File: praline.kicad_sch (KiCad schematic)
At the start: 0 parts

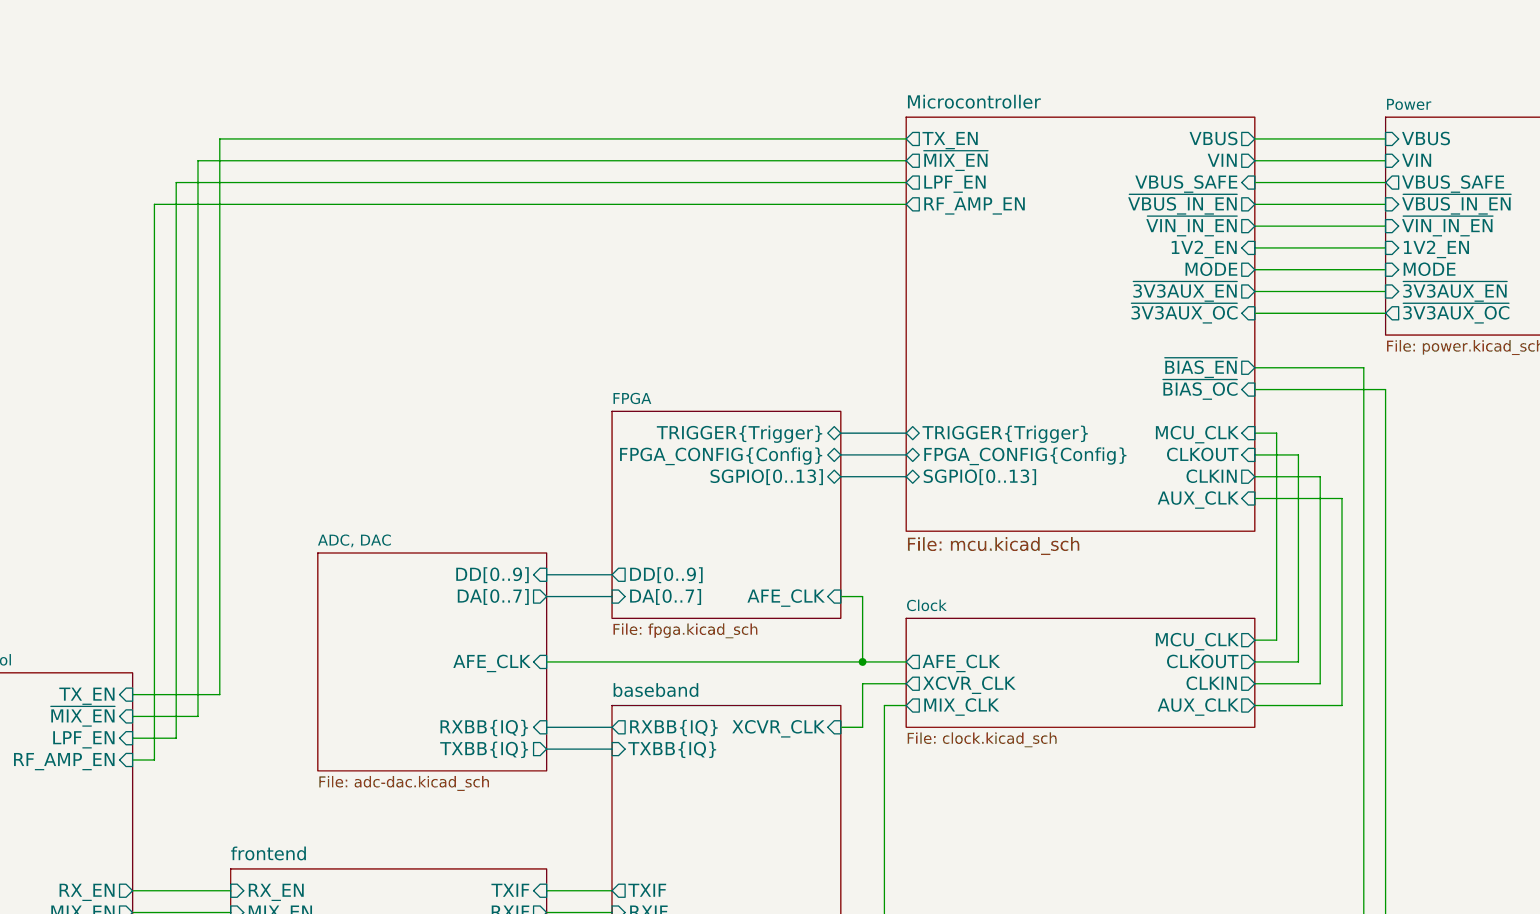
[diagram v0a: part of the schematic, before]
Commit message: Add Type-C controller
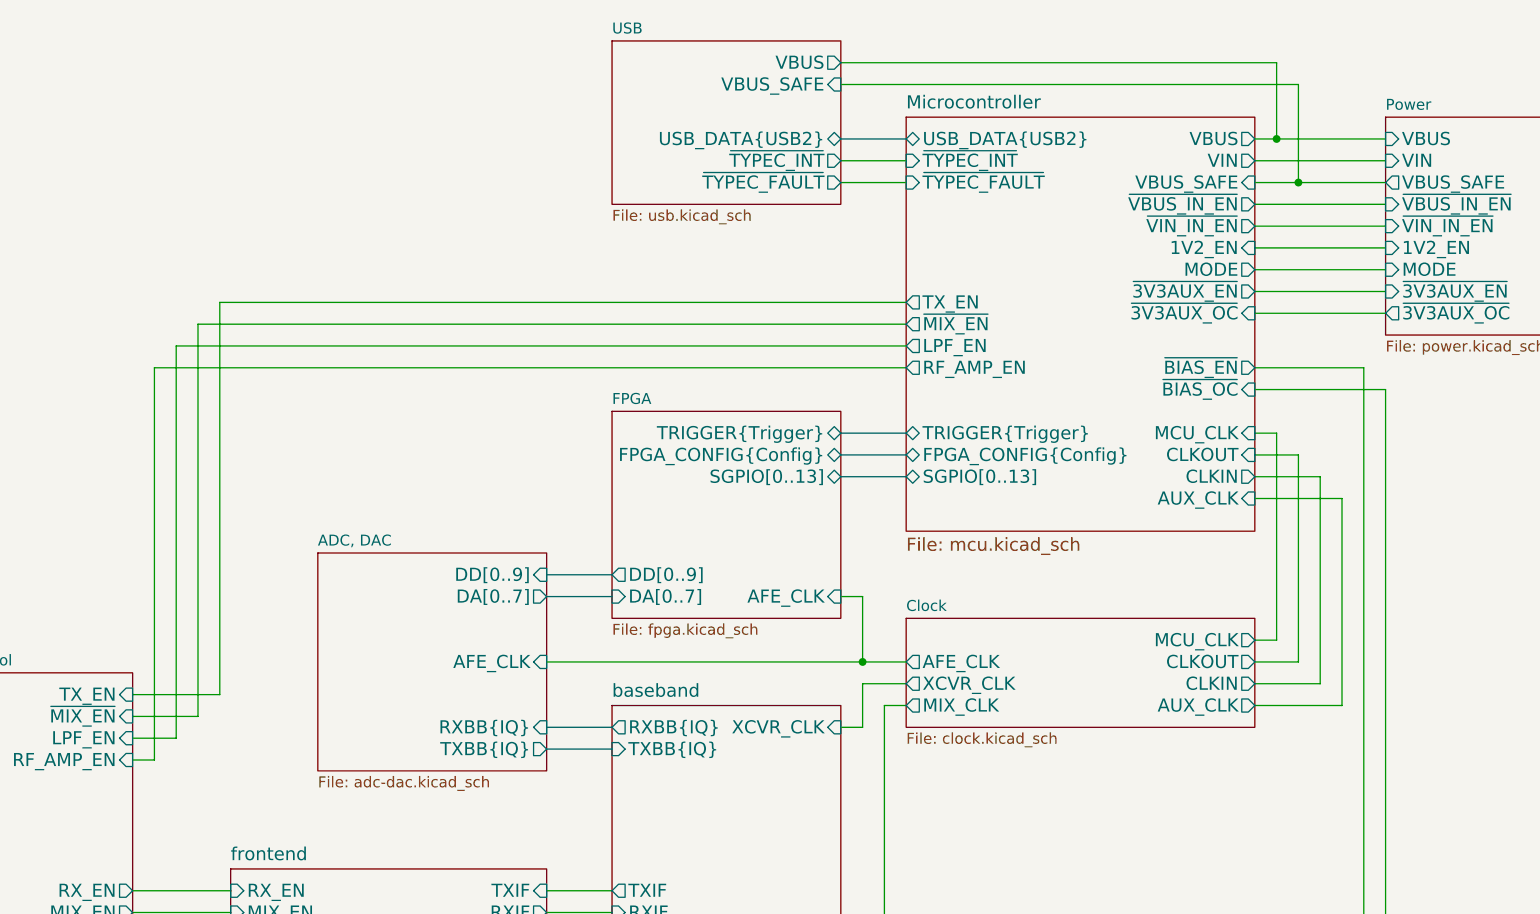
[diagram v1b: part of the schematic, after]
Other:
- added sheet USB (usb.kicad_sch)
- sheet Microcontroller ports: added USB_DATA{USB2}, ~{TYPEC_FAULT}, ~{TYPEC_INT}; removed none

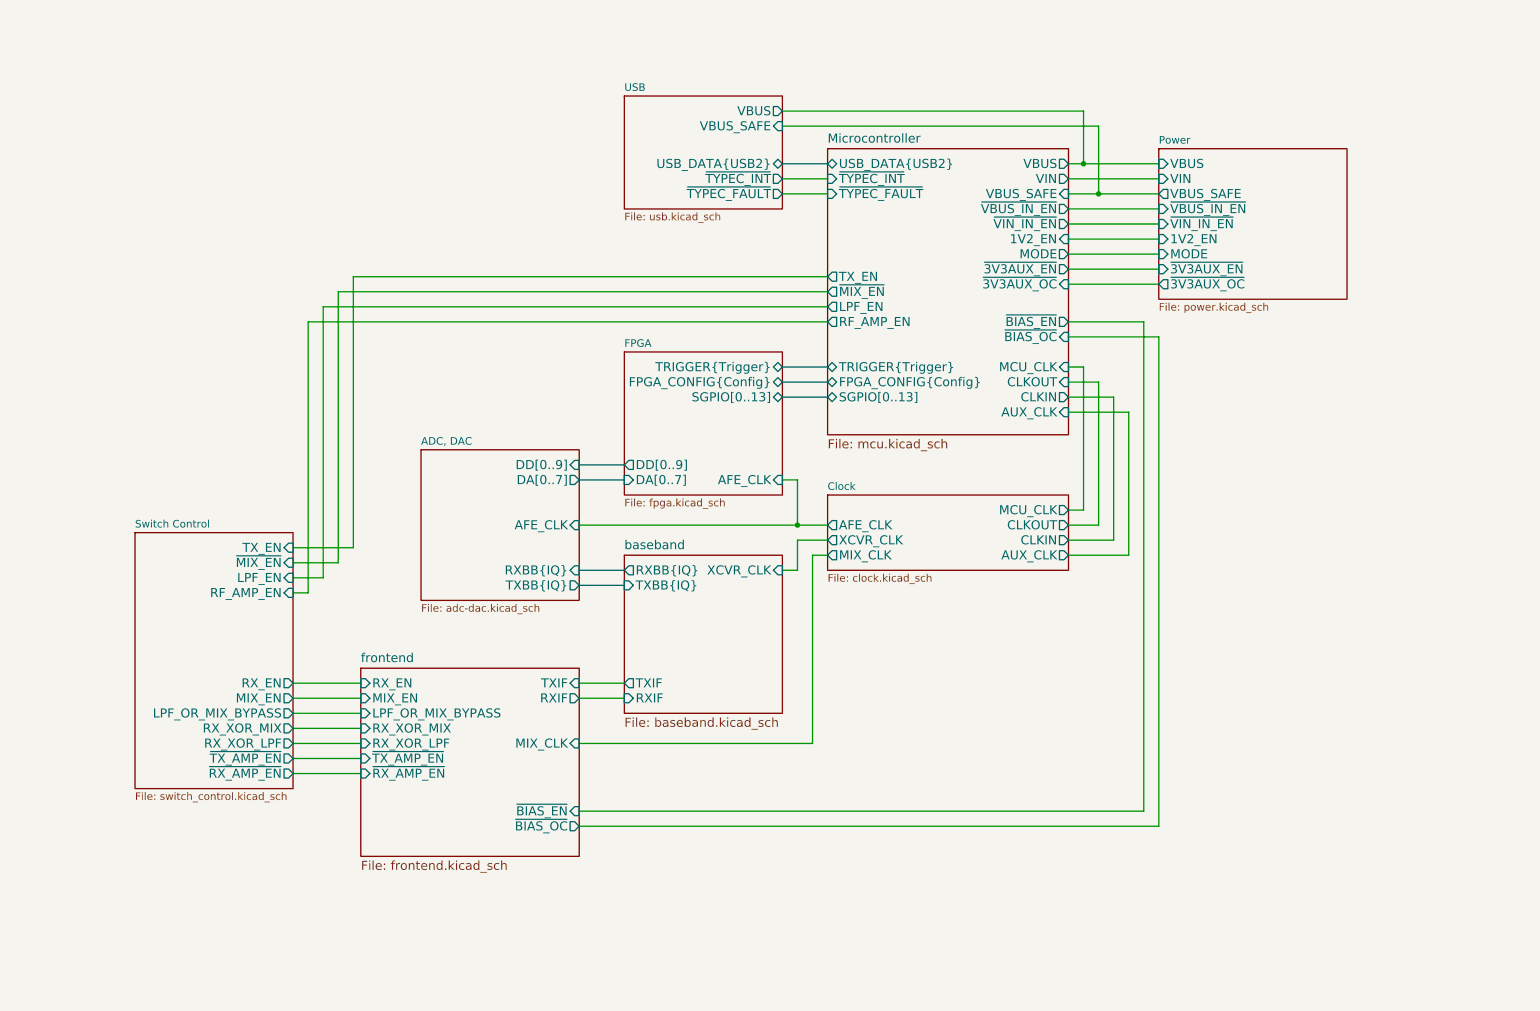
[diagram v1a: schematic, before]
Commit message: Change U17 from MAX2837 to MAX2831
Update version to 0.2.0+
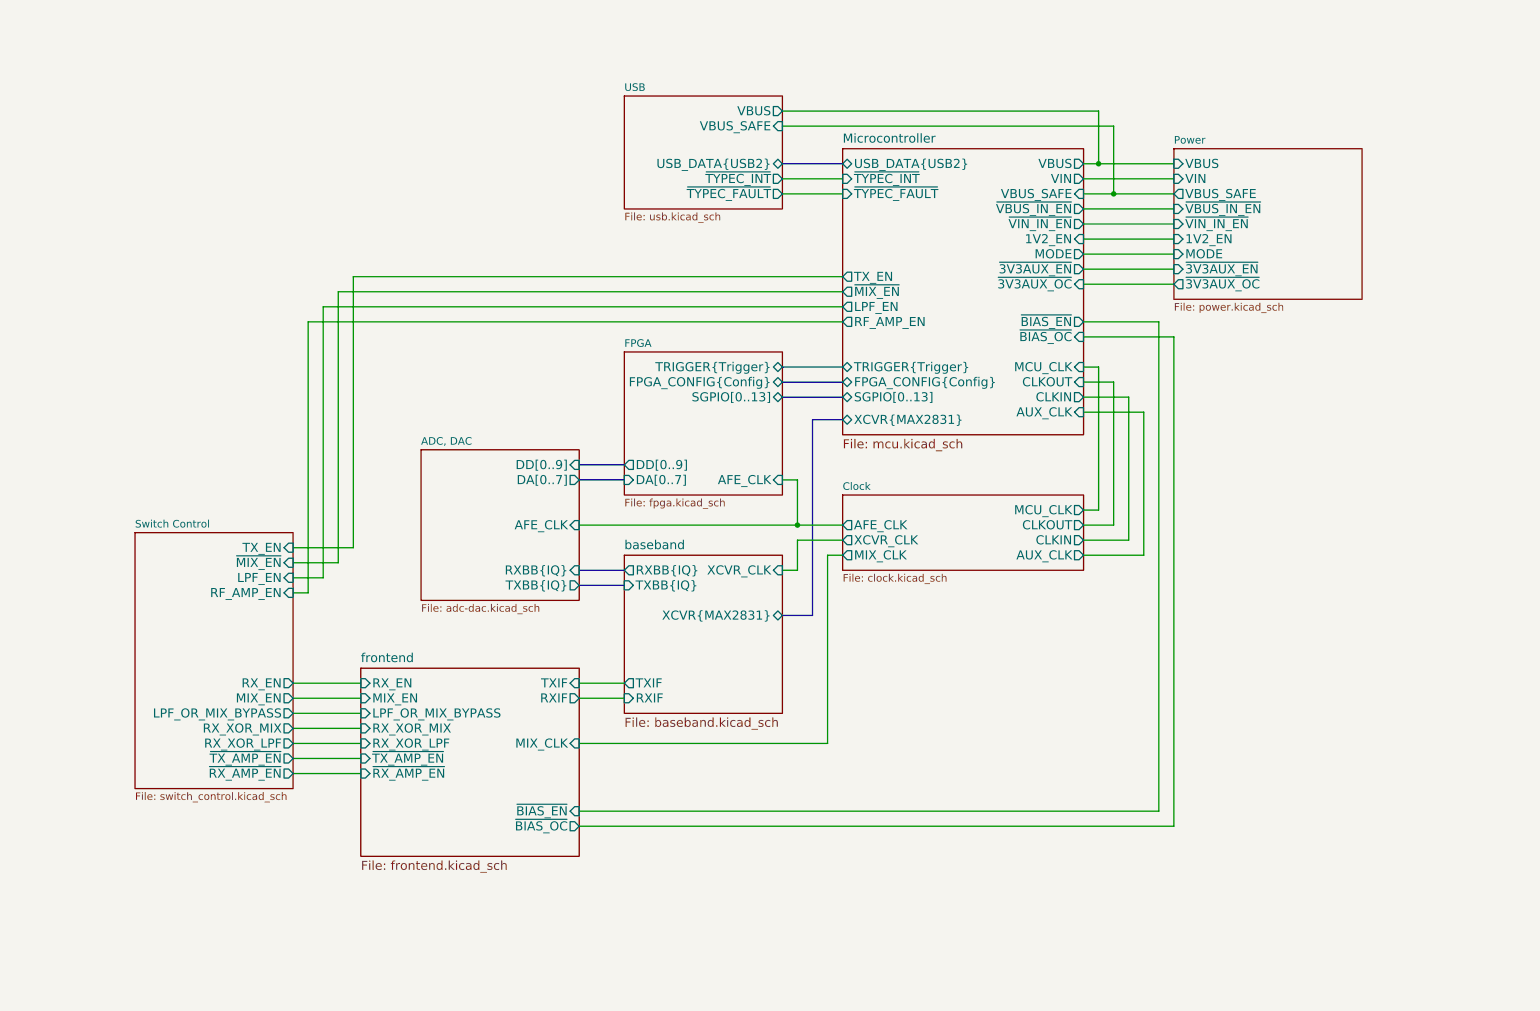
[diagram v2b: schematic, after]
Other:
- sheet Microcontroller ports: added XCVR{MAX2831}; removed none
- sheet baseband ports: added XCVR{MAX2831}; removed none

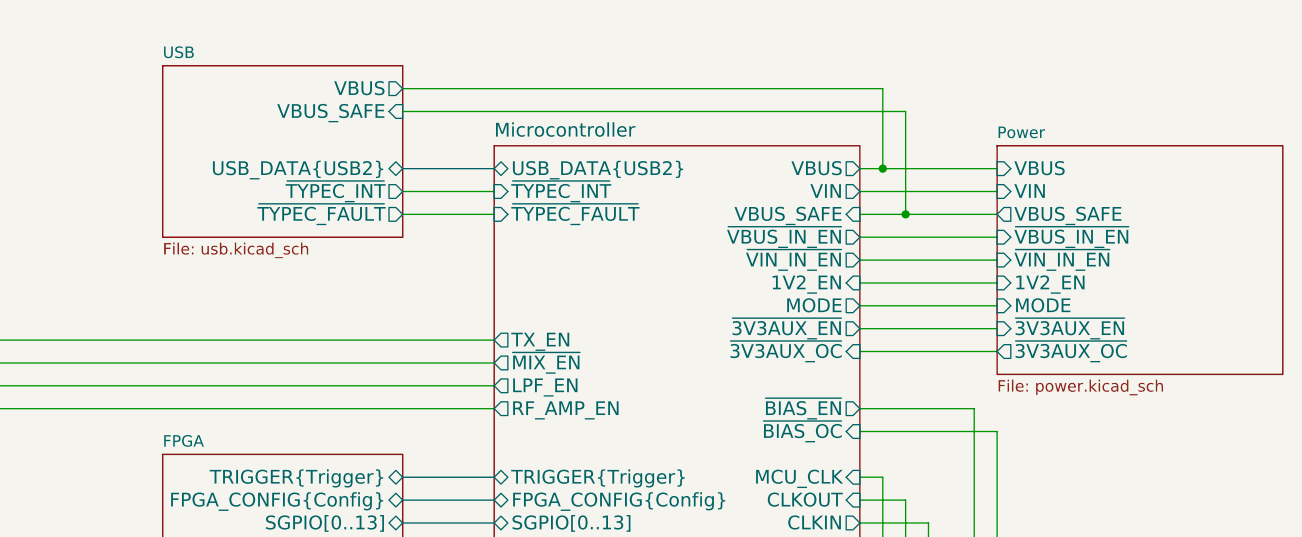
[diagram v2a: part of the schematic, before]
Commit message: Change Type-C controller U29 to HUSB328
- Update USB TVS
- Improve USB differential impedance
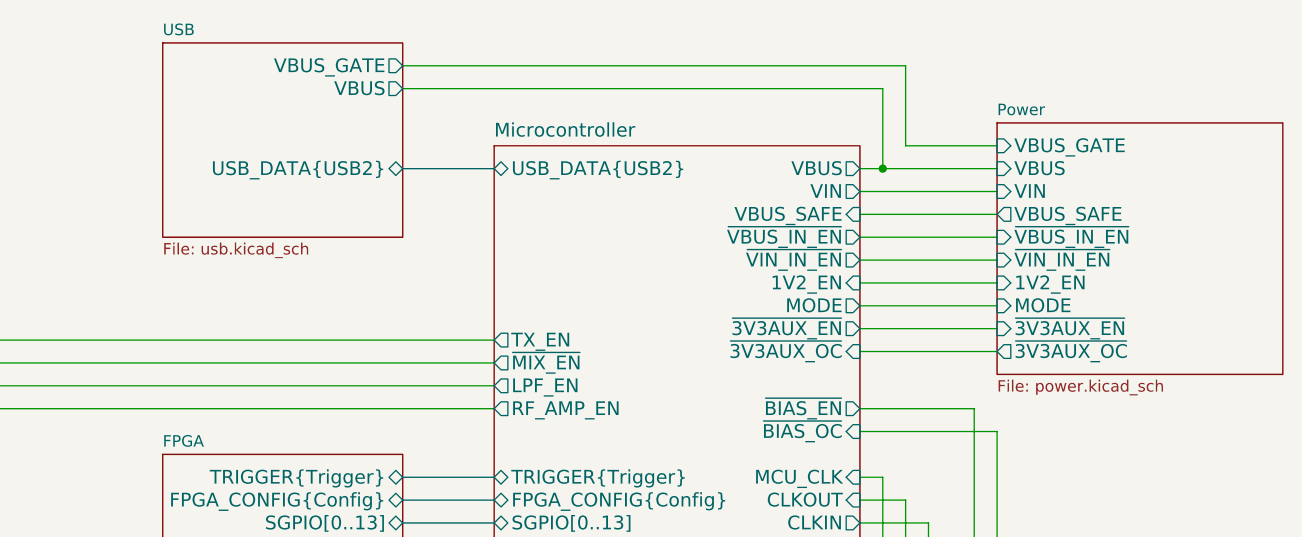
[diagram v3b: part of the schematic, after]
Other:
- sheet Microcontroller ports: added none; removed ~{TYPEC_FAULT}, ~{TYPEC_INT}
- sheet Power ports: added VBUS_GATE; removed none
- sheet USB ports: added VBUS_GATE; removed VBUS_SAFE, ~{TYPEC_FAULT}, ~{TYPEC_INT}
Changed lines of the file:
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@@
-	)
-	(junction
-		(at 210.82 44.45)
-		(diameter 0)
-		(color 0 0 0 0)
 	)
 	(junction
@@
 		)
 	)
+	(wire
+		(pts
+			(xy 210.82 36.83) (xy 220.98 36.83)
+		)
+		(stroke
+			(width 0)
+			(type default)
+		)
+	)
 	(bus
 		(pts
@@
 		)
 	)
-	(wire
-		(pts
-			(xy 154.94 41.91) (xy 165.1 41.91)
-		)
-		(stroke
-			(width 0)
-			(type default)
-		)
-	)
 	(bus
 		(pts
@@
 	(wire
 		(pts
-			(xy 210.82 33.02) (xy 210.82 44.45)
-		)
-		(stroke
-			(width 0)
-			(type default)
-		)
-	)
-	(wire
-		(pts
 			(xy 157.48 102.87) (xy 157.48 107.95)
 		)
@@
 	(wire
 		(pts
-			(xy 210.82 44.45) (xy 220.98 44.45)
-		)
-		(stroke
-			(width 0)
-			(type default)
-		)
-	)
-	(wire
-		(pts
 			(xy 120.65 127) (xy 128.27 127)
 		)
@@
 	(wire
 		(pts
+			(xy 210.82 27.94) (xy 210.82 36.83)
+		)
+		(stroke
+			(width 0)
+			(type default)
+		)
+	)
+	(wire
+		(pts
 			(xy 157.48 92.71) (xy 157.48 100.33)
 		)
@@
 		)
 	)
-	(wire
-		(pts
-			(xy 154.94 44.45) (xy 165.1 44.45)
-		)
-		(stroke
-			(width 0)
-			(type default)
-		)
-	)
 	(bus
 		(pts
@@
 	(wire
 		(pts
-			(xy 154.94 33.02) (xy 210.82 33.02)
-		)
-		(stroke
-			(width 0)
-			(type default)
-		)
-	)
-	(wire
-		(pts
-			(xy 205.74 44.45) (xy 210.82 44.45)
+			(xy 154.94 27.94) (xy 210.82 27.94)
+		)
+		(stroke
+			(width 0)
+			(type default)
+		)
+	)
+	(wire
+		(pts
+			(xy 205.74 44.45) (xy 220.98 44.45)
 		)
 		(stroke
@@
 			)
 		)
-		(pin "~{TYPEC_INT}" input
-			(at 165.1 41.91 180)
-			(effects
-				(font
-					(size 1.524 1.524)
-				)
-				(justify left)
-			)
-		)
-		(pin "~{TYPEC_FAULT}" input
-			(at 165.1 44.45 180)
-			(effects
-				(font
-					(size 1.524 1.524)
-				)
-				(justify left)
-			)
-		)
 		(pin "USB_DATA{USB2}" bidirectional
 			(at 165.1 39.37 180)
@@
 	)
 	(sheet
-		(at 220.98 36.83)
-		(size 31.75 25.4)
+		(at 220.98 34.29)
+		(size 31.75 27.94)
 		(fields_autoplaced yes)
 		(stroke
@@
 		)
 		(property "Sheetname" "Power"
-			(at 220.98 36.1184 0)
+			(at 220.98 33.5784 0)
 			(effects
 				(font
@@
 		(pin "~{3V3AUX_OC}" output
 			(at 220.98 59.69 180)
+			(effects
+				(font
+					(size 1.524 1.524)
+				)
+				(justify left)
+			)
+		)
+		(pin "VBUS_GATE" input
+			(at 220.98 36.83 180)
 			(effects
 				(font
@@
 	)
 	(sheet
-		(at 128.27 27.94)
-		(size 26.67 19.05)
+		(at 128.27 25.4)
+		(size 26.67 21.59)
 		(fields_autoplaced yes)
 		(stroke
@@
 		)
 		(property "Sheetname" "USB"
-			(at 128.27 27.2284 0)
+			(at 128.27 24.6884 0)
 			(effects
 				(font
@@
 			)
 		)
-		(pin "~{TYPEC_INT}" output
-			(at 154.94 41.91 0)
-			(effects
-				(font
-					(size 1.524 1.524)
-				)
-				(justify right)
-			)
-		)
 		(pin "USB_DATA{USB2}" bidirectional
 			(at 154.94 39.37 0)
@@
 			)
 		)
-		(pin "VBUS_SAFE" input
-			(at 154.94 33.02 0)
-			(effects
-				(font
-					(size 1.524 1.524)
-				)
-				(justify right)
-			)
-		)
-		(pin "~{TYPEC_FAULT}" output
-			(at 154.94 44.45 0)
-			(effects
-				(font
+		(pin "VBUS_GATE" output
+			(at 154.94 27.94 0)
+			(effects
+				(font
